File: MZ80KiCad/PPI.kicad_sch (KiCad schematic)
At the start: 31 parts, among them J3 to CASETTE, J4 KEYBOARD, Q1 2SA505Y, Q2 2SC373, Q3 2SC373, Q4 2SC373, Q5 373, U1 ICM7555xP, U2 74LS74, U24 74LS00, U3 7406, U4 74LS14, U5 8255, U6 74LS145

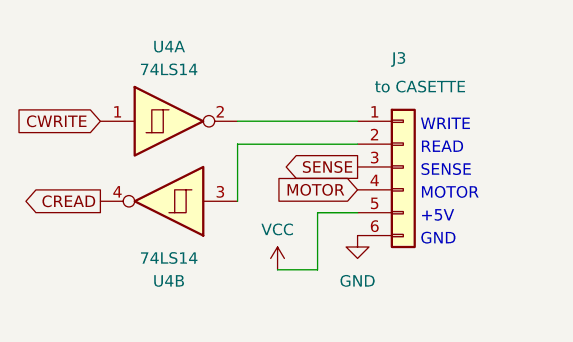
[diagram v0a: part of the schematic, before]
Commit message: fix U47 pin18 pin19
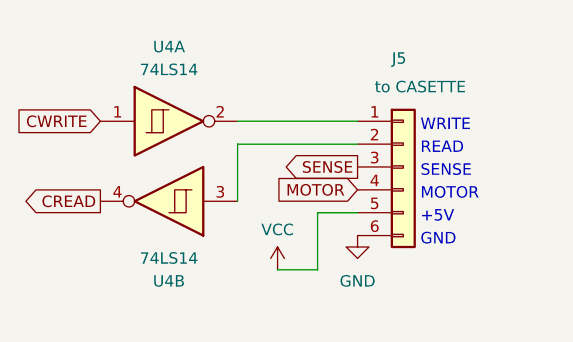
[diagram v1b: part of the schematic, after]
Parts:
- renumbered J3 to J5
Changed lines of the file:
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@@
   (symbol (lib_id "power:GND") (at 260.985 42.545 0) (unit 1)
     (in_bom yes) (on_board yes) (dnp no) (fields_autoplaced)
-    (property "Reference" "#PWR0197" (at 260.985 48.895 0)
+    (property "Reference" "#PWR0214" (at 260.985 48.895 0)
       (effects (font (size 1.27 1.27)) hide)
     )
@@
     (instances
       (project "MZ80"
-        (path "/4c07815a-c510-44da-af98-4d055fa8c080/655b2a57-bfc0-4e66-85e7-e1ccf742c0b5"
-          (reference "#PWR0197") (unit 1)
-        )
         (path "/4c07815a-c510-44da-af98-4d055fa8c080/7b3a55ce-66ff-4227-8a4d-d2f73cb0a8bf"
           (reference "#PWR0214") (unit 1)
@@
   (symbol (lib_id "Connector_Generic:Conn_01x06") (at 266.065 34.925 0) (unit 1)
     (in_bom yes) (on_board yes) (dnp no)
-    (property "Reference" "J3" (at 264.795 22.86 0)
+    (property "Reference" "J5" (at 264.795 22.86 0)
       (effects (font (size 1.27 1.27)) (justify left))
     )
@@
     (instances
       (project "MZ80"
-        (path "/4c07815a-c510-44da-af98-4d055fa8c080/655b2a57-bfc0-4e66-85e7-e1ccf742c0b5"
-          (reference "J3") (unit 1)
-        )
         (path "/4c07815a-c510-44da-af98-4d055fa8c080/7b3a55ce-66ff-4227-8a4d-d2f73cb0a8bf"
           (reference "J5") (unit 1)
